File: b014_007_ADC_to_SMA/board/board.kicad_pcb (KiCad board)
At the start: 2 copper layers, 21 x 13 mm, 3 parts, among them J1 Conn_Coaxial, J2 007_ADC_2x2

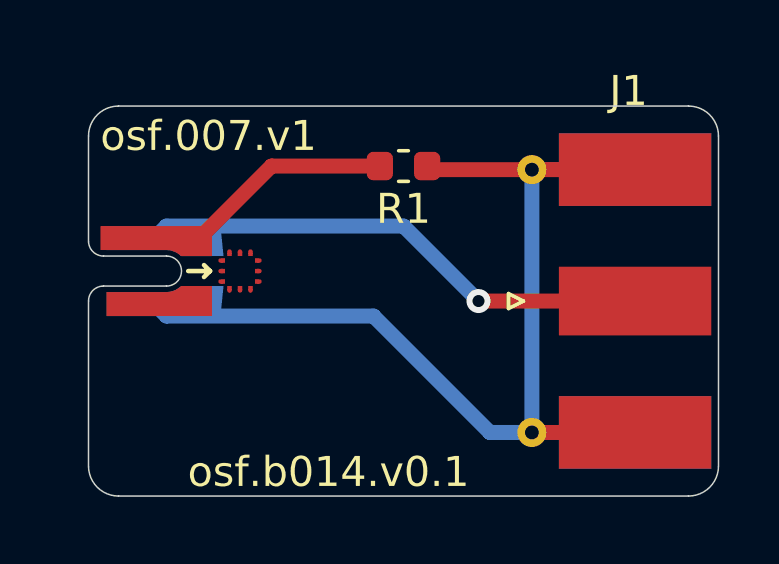
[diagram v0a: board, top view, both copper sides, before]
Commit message: updated analog connector footprint
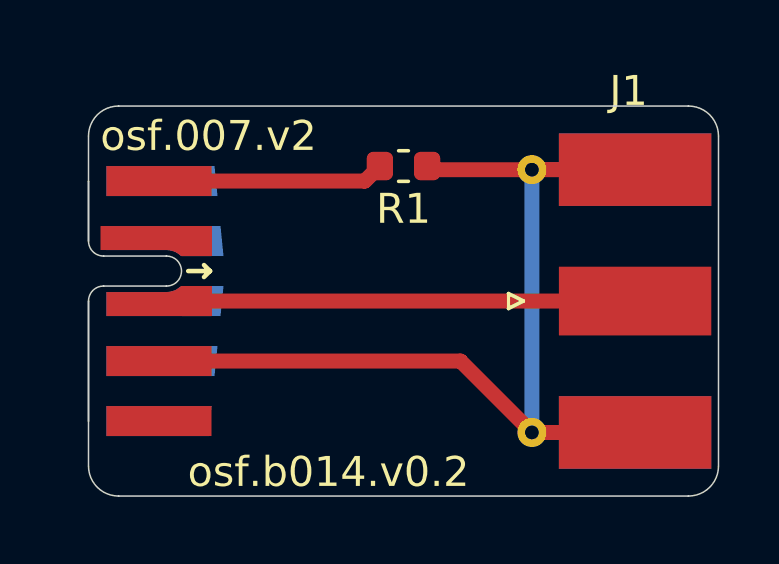
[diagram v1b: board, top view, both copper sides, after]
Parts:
- J2: footprint on_edge:on_edge_2x02_device -> on_edge:on_edge_2x05_device
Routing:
- net Net-(J1-Pad1): track 17.4 -> 14.6 mm, vias 1 -> 0
- net Net-(J1-Pad2): track 34.0 -> 32.9 mm
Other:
- board text added: "osf.007.v2"
- board text added: "osf.b014.v0.2"
- board text removed: "osf.007.v1"
- board text removed: "osf.b014.v0.1"

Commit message: updated to kicad 6 (#54)
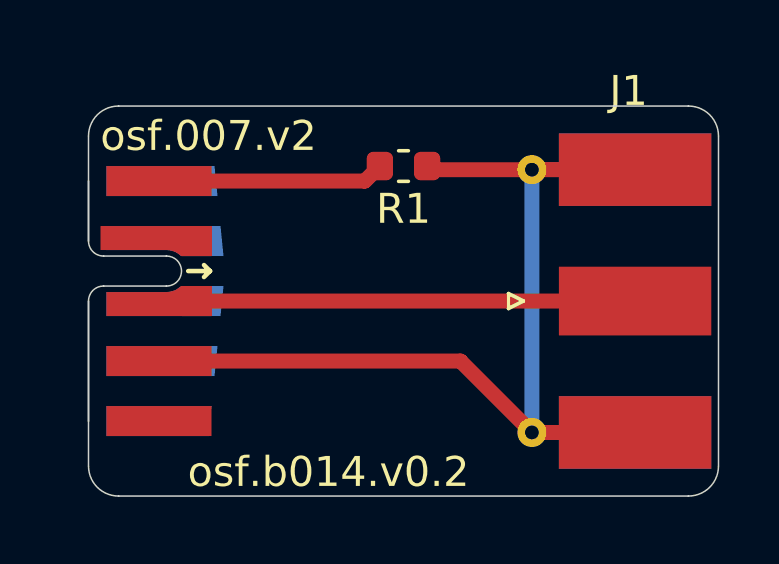
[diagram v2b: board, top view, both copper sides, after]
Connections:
- J2 pad 10: (no net) -> unconnected-(J2-Pad10)
- J2 pad 2: (no net) -> unconnected-(J2-Pad2)
- J2 pad 5: (no net) -> unconnected-(J2-Pad5)
- J2 pad 6: (no net) -> unconnected-(J2-Pad6)
- J2 pad 9: (no net) -> unconnected-(J2-Pad9)
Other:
- net class Default removed
